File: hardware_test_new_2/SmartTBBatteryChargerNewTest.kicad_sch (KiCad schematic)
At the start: 130 parts, among them J3 XT60_MALE, J7 Conn_SWD, J8 Conn_01x02, Q3 AO3400A, Q4 BSC070N10NS5, U1 RY8411, U2 RS3236, U3 RY8411, U4 STM32G474RBTx, U5 INA180A1, U9 INA240A1PW, Y3 CSTCE8M

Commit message: New test channel schematic
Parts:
- removed C100, C101, C102, C103, C43, C44, C50, C51, C52, C58, C92, C93, C94, C95, C96, C97, C98, C99: 100n, Capacitor_SMD:C_0603_1608Metric, symbol Device:C
- removed C40, C42, C49: 100u, Capacitor_THT:CP_Radial_D6.3mm_P2.50mm, symbol Device:C_Polarized
- removed C45, C46, C59: 10u, Capacitor_SMD:C_1206_3216Metric, symbol Device:C
- removed D18, D19, D20, D21, D22, D23, D24, D25, D26, D27, D28, D29: WS2812B-2020, LED_SMD:LED_WS2812B-2020_PLCC4_2.0x2.0mm, symbol LED:WS2812B-2020
- removed D3: D_Schottky, Diode_SMD:D_PowerDI-5, symbol Device:D_Schottky
- removed F3: 5A, Fuse:Fuse_1206_3216Metric, symbol Device:Fuse
- removed J3: XT60_MALE, Connector_AMASS:AMASS_XT60-M_1x02_P7.20mm_Vertical, symbol Connector_Generic:Conn_01x02
- removed L4: 47u, Inductor_SMD:L_Coilcraft_MSS1260-XXX, symbol Device:L
- removed Q4: BSC070N10NS5, Package_TO_SOT_SMD:TDSON-8-1, symbol Transistor_FET:BSC070N10NS5
- removed R14: 10k, Resistor_SMD:R_0603_1608Metric, symbol Device:R
- removed R15: 90k, Resistor_SMD:R_0603_1608Metric, symbol Device:R
- removed R22: 33R, Resistor_SMD:R_0603_1608Metric, symbol Device:R
- removed R23: 4m, Resistor_SMD:R_Shunt_Vishay_WSK2512_6332Metric_T1.19mm, symbol Device:R_Shunt
- removed R28: 1R, Resistor_SMD:R_0603_1608Metric, symbol Device:R
- removed R5: 10m, Resistor_SMD:R_Shunt_Vishay_WSK2512_6332Metric_T1.19mm, symbol Device:R_Shunt
- removed U5: INA180A1, Package_TO_SOT_SMD:SOT-23-5, symbol Amplifier_Current:INA180A1
- removed U9: INA240A1PW, Package_SO:TSSOP-8_4.4x3mm_P0.65mm, symbol Amplifier_Current:INA240A1PW
- added C22: 10u, Capacitor_SMD:C_1206_3216Metric, symbol Device:C_Small
- added C24: 100n, Capacitor_SMD:C_0603_1608Metric, symbol Device:C_Small
- added D10: K34, Diode_SMD:D_SOD-123F, symbol Device:D_Schottky
- added U6: FD6288Q, Package_DFN_QFN:QFN-24-1EP_4x4mm_P0.5mm_EP2.7x2.7mm, symbol AEX7 Others:FD6288Q
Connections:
- net +10V: now also C22.1, D10.2 (A), U6.4 (VCC)
- net CHA_HG: now also U6.19 (HO1)
- net CHA_SW: now also C24.2, U6.18 (VS1)
- net GND: now also C22.2, U6.25 (EP), U6.6 (COM)
- net VPP: now also F8.1
- new net: C24.1, D10.1 (K), U6.20 (VB1)
- new net: U6.21 (NC), U6.5 (NC), U6.7 (NC), U6.8 (NC)
- new net CHA1_DRVH: U6.22 (HIN1)
- new net CHA2_DRVH: U6.23 (HIN2)
- new net CHB1_DRVH: U6.24 (HIN3)
- no-connect marks 36 -> 41
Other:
- added sheet ChannelA1 (channel1.kicad_sch)
- added sheet ChannelA2 (channel1.kicad_sch)
- moved on the sheet: JP1

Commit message: test2 schematic
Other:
- added sheet ChannelB1 (channel1.kicad_sch)
- added sheet ChannelB2 (channel1.kicad_sch)
- added sheet ChannelC1 (channel1.kicad_sch)
- added sheet ChannelC2 (channel1.kicad_sch)

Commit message: test2 schematic should ok
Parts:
- removed D4, D5, D6: LED, LED_SMD:LED_0603_1608Metric, symbol Device:LED
- removed Y3: CSTCE8M, Crystal:Resonator_SMD_Murata_CSTxExxV-3Pin_3.0x1.1mm_HandSoldering, symbol Device:Resonator
- added C101, C102, C103, C104, C105, C106, C107, C108, C109, C37, C38, C39: 100n, Capacitor_SMD:C_0603_1608Metric, symbol Device:C
- added C110, C111, C31, C32, C34, C35, C36: 100n, Capacitor_SMD:C_0603_1608Metric, symbol Device:C_Small
- added C33: 10u, Capacitor_SMD:C_1206_3216Metric, symbol Device:C_Small
- added D18, D19, D20, D21, D22: K34, Diode_SMD:D_SOD-123F, symbol Device:D_Schottky
- added D23, D24, D25, D26, D27, D28: LED_BLUE, LED_SMD:LED_0603_1608Metric, symbol Device:LED
- added D29, D30, D31, D4, D5, D6: WS2812B, LED_SMD:LED_WS2812B_PLCC4_5.0x5.0mm_P3.2mm, symbol LED:WS2812B
- added R12, R54, R56: 10k, Resistor_SMD:R_0603_1608Metric, symbol Device:R
- added R53, R55, R57, R64: 33, Resistor_SMD:R_0603_1608Metric, symbol Device:R
- added R58, R59, R60, R61, R62, R63: 2.2k, Resistor_SMD:R_0603_1608Metric, symbol Device:R
- added RN1, RN2: R_Pack04, Resistor_SMD:R_Array_Convex_4x0603, symbol Device:R_Pack04
- added SW1, SW2, SW3, SW4, SW5, SW6: SW_Push, Button_Switch_SMD:SW_SPST_SKQG_WithStem, symbol Switch:SW_Push
- added U12: FD6288Q, Package_DFN_QFN:QFN-24-1EP_4x4mm_P0.5mm_EP2.7x2.7mm, symbol AEX7 Others:FD6288Q
- J8: footprint Connector_AMASS:AMASS_XT30U-M_1x02_P5.0mm_Vertical -> Connector_AMASS:AMASS_XT60-M_1x02_P7.20mm_Vertical
- R13, R17: value 33r -> 33
- R16: value 33r -> 10k
- R3: value 53.6k -> 54.7k
- R30, R32: value 2.2k -> 10k
- R31: value 2.2k -> 33
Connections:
- net CHA_HG is gone; now on net CHA1_HG: U6.19 (HO1)
- net CHA_SW is gone; now on net CHA1_SW: C24.2, U6.18 (VS1)
- net DRV_CHA1 is gone; now on net +3.3V: R16.1
- net DRV_CHA2 is gone; now on net BTN1: R13.1
- net DRV_CHB is gone; now on net BTN2: R17.1
- net ISENSE_INPUT is gone; now on net VSENSE_INPUT: U4.8 (PC0)
- net +10V: now also C110.1, C111.1, C33.1, D18.2 (A), D19.2 (A), D20.2 (A), D21.2 (A), D22.2 (A), U12.4 (VCC)
- net +3.3V: now also R30.1, R32.1, R12.1, R54.1, R56.1
- net +5V: now also C104.2, C105.2, C106.2, C107.2, C108.2, C109.2, D29.1 (VDD), D30.1 (VDD), D31.1 (VDD), D4.1 (VDD), D5.1 (VDD), D6.1 (VDD)
- net CHA1_DRVH: now also U4.42 (PA8), R58.1, RN2.1 (R1.1); no longer U6.22 (HIN1)
- net CHA2_DRVH: now also U4.43 (PA9), R59.1, RN2.2 (R2.1); no longer U6.23 (HIN2)
- net CHA2_HG: now also U6.16 (HO2)
- net CHA2_SW: now also U6.15 (VS2), C31.2
- net CHB1_DRVH: now also U4.44 (PA10), R60.1, RN2.3 (R3.1); no longer U6.24 (HIN3)
- net CHB1_HG: now also U6.13 (HO3)
- net CHB1_SW: now also U6.12 (VS3), C32.2
- net CHB2_HG: now also U12.19 (HO1)
- net CHB2_SW: now also C34.2, U12.18 (VS1)
- net CHC1_HG: now also U12.16 (HO2)
- net CHC1_SW: now also C35.2, U12.15 (VS2)
- net CHC2_HG: now also U12.13 (HO3)
- net CHC2_SW: now also C36.2, U12.12 (VS3)
- net GND: now also C101.1, C102.1, C103.1, C104.1, C105.1, C106.1, C107.1, C108.1, C109.1, C110.2, C111.2, C33.2, C37.1, C38.1, C39.1, D23.1 (K), D24.1 (K), D25.1 (K), D26.1 (K), D27.1 (K), D28.1 (K), D29.3 (VSS), D30.3 (VSS), D31.3 (VSS), D4.3 (VSS), D5.3 (VSS), D6.3 (VSS), SW1.2, SW2.2, SW3.2, SW4.2, SW5.2, SW6.2, U12.25 (EP), U12.6 (COM)
- net RGB_DATA: now also U4.57 (PB4), R64.1; no longer U4.45 (PA11)
- net VSENSE_INPUT: no longer U4.35 (PB13)
- net CHB2_VS: now reaches U4.11 (PC3)
- net CHB1_VS: now reaches U4.12 (PA0)
- net CHA2_VS: now reaches U4.13 (PA1)
- net CHA1_VS: now reaches U4.14 (PA2)
- net CHC2_IS: now reaches U4.19 (PA5)
- net CHC1_IS: now reaches U4.20 (PA6)
- net CHB1_IS: now reaches U4.22 (PC4)
- net CHA2_IS: now reaches U4.23 (PC5)
- net CHA1_IS: now reaches U4.26 (PB2)
- net CHC2_DRVH: now reaches U4.34 (PB12)
- net CHC2_DRVH: now also R63.1, RN1.3 (R3.1)
- net BTN6: now reaches U4.55 (PD2)
- net BTN6: now also C103.2, R57.1
- net BTN5: now reaches U4.56 (PB3)
- net BTN5: now also C102.2, R55.1
- net BTN4: now reaches U4.58 (PB5)
- net BTN4: now also C101.2, R53.1
- net BTN3: now reaches U4.59 (PB6)
- net BTN3: now also R31.1, C39.2
- net BTN2: now reaches U4.60 (PB7)
- net BTN2: now also C38.2
- net BTN1: now reaches U4.62 (PB9)
- net BTN1: now also C37.2
- net at U6.14 (VB3): now also C32.1, D19.1 (K)
- net at U6.17 (VB2): now also C31.1, D18.1 (K)
- net at R31.2: now also R30.2, SW3.1
- net at R32.2: now also R53.2, SW4.1
- net ISENSE_CHA renamed CHC1_VS
- net ISENSE_CHB renamed CHC2_VS
- net VSENSE_CHA renamed CHB2_IS
- net VSENSE_CHB: no longer names the net of U4.24 (PB0)
- new net: R56.2, R57.2, SW6.1
- new net: R16.2, R17.2, SW2.1
- new net: C36.1, D22.1 (K), U12.14 (VB3)
- new net: C34.1, D20.1 (K), U12.20 (VB1)
- new net: D25.2 (A), R60.2
- new net: D27.2 (A), R62.2
- new net: C35.1, D21.1 (K), U12.17 (VB2)
- new net: D29.2 (DOUT), D30.4 (DIN)
- new net: D29.4 (DIN), D6.2 (DOUT)
- new net: D4.2 (DOUT), D5.4 (DIN)
- new net: D4.4 (DIN), R64.2
- new net: D28.2 (A), R63.2
- new net: RN2.8 (R1.2), U6.22 (HIN1)
- new net: RN2.7 (R2.2), U6.23 (HIN2)
- new net: RN2.6 (R3.2), U6.24 (HIN3)
- new net: RN1.6 (R3.2), U12.24 (HIN3)
- new net: RN1.7 (R2.2), U12.23 (HIN2)
- new net: RN1.8 (R1.2), U12.22 (HIN1)
- new net: D26.2 (A), R61.2
- new net: D24.2 (A), R59.2
- new net: D5.2 (DOUT), D6.4 (DIN)
- new net: R12.2, R13.2, SW1.1
- new net: U12.21 (NC), U12.5 (NC), U12.7 (NC), U12.8 (NC)
- new net: D23.2 (A), R58.2
- new net: R54.2, R55.2, SW5.1
- new net: D30.2 (DOUT), D31.4 (DIN)
- new net CHB2_DRVH: R61.1, RN1.1 (R1.1), U4.45 (PA11)
- new net CHC1_DRVH: R62.1, RN1.2 (R2.1), U4.35 (PB13)
- no-connect marks 41 -> 44
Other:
- sheet ChannelA1 ports: added CH_VOUT; removed none
- sheet ChannelA2 ports: added CH_VOUT; removed none
- sheet ChannelB1 ports: added CH_VOUT; removed none
- sheet ChannelB2 ports: added CH_VOUT; removed none
- sheet ChannelC1 ports: added CH_VOUT; removed none
- sheet ChannelC2 ports: added CH_VOUT; removed none
- moved on the sheet: BZ1, C22, C24, C53, C54, C55, C56, D10, D9, F8, FB1, J8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

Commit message: layout half done
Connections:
- net +3.3V: no longer C90.2, C91.2, U4.28 (VREF+)
- new net VREF: C90.2, C91.2, U4.28 (VREF+)
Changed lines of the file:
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@@
 	(wire
 		(pts
-			(xy 60.96 45.72) (xy 57.15 45.72)
-		)
-		(stroke
-			(width 0)
-			(type default)
-		)
-	)
-	(wire
-		(pts
 			(xy 186.69 254) (xy 193.04 254)
 		)
@@
 	(wire
 		(pts
+			(xy 57.15 45.72) (xy 58.42 45.72)
+		)
+		(stroke
+			(width 0)
+			(type default)
+		)
+	)
+	(wire
+		(pts
 			(xy 36.83 30.48) (xy 34.29 30.48)
 		)
@@
 		)
 	)
+	(label "VREF"
+		(at 58.42 45.72 0)
+		(effects
+			(font
+				(size 1.27 1.27)
+			)
+			(justify left bottom)
+		)
+	)
 	(global_label "CHC2_SW"
 		(shape input)
@@
 					(unit 1)
 				)
-			)
-		)
-	)
-	(symbol
-		(lib_id "power:+3.3V")
-		(at 60.96 45.72 0)
-		(unit 1)
-		(exclude_from_sim no)
-		(in_bom yes)
-		(on_board yes)
-		(dnp no)
-		(fields_autoplaced yes)
-		(property "Reference" "#PWR018"
-			(at 60.96 49.53 0)
-			(effects
-				(font
-					(size 1.27 1.27)
-				)
-				(hide yes)
-			)
-		)
-		(property "Value" "+3.3V"
-			(at 60.96 40.64 0)
-			(effects
-				(font
-					(size 1.27 1.27)
-				)
-			)
-		)
-		(property "Footprint" ""
-			(at 60.96 45.72 0)
-			(effects
-				(font
-					(size 1.27 1.27)
-				)
-				(hide yes)
-			)
-		)
-		(property "Datasheet" ""
-			(at 60.96 45.72 0)
-			(effects
-				(font
-					(size 1.27 1.27)
-				)
-				(hide yes)
-			)
-		)
-		(property "Description" "Power symbol creates a global label with name \"+3.3V\""
-			(at 60.96 45.72 0)
-			(effects
-				(font
-					(size 1.27 1.27)
-				)
-				(hide yes)
-			)
-		)
-		(pin "1"
-		)
-		(instances
-			(project "SmartTBBatteryChargerNewTest"
-				(path "/2e05ddd5-7934-49df-b3d1-7d213e2935b6"
-					(reference "#PWR018")
-					(unit 1)
-				)

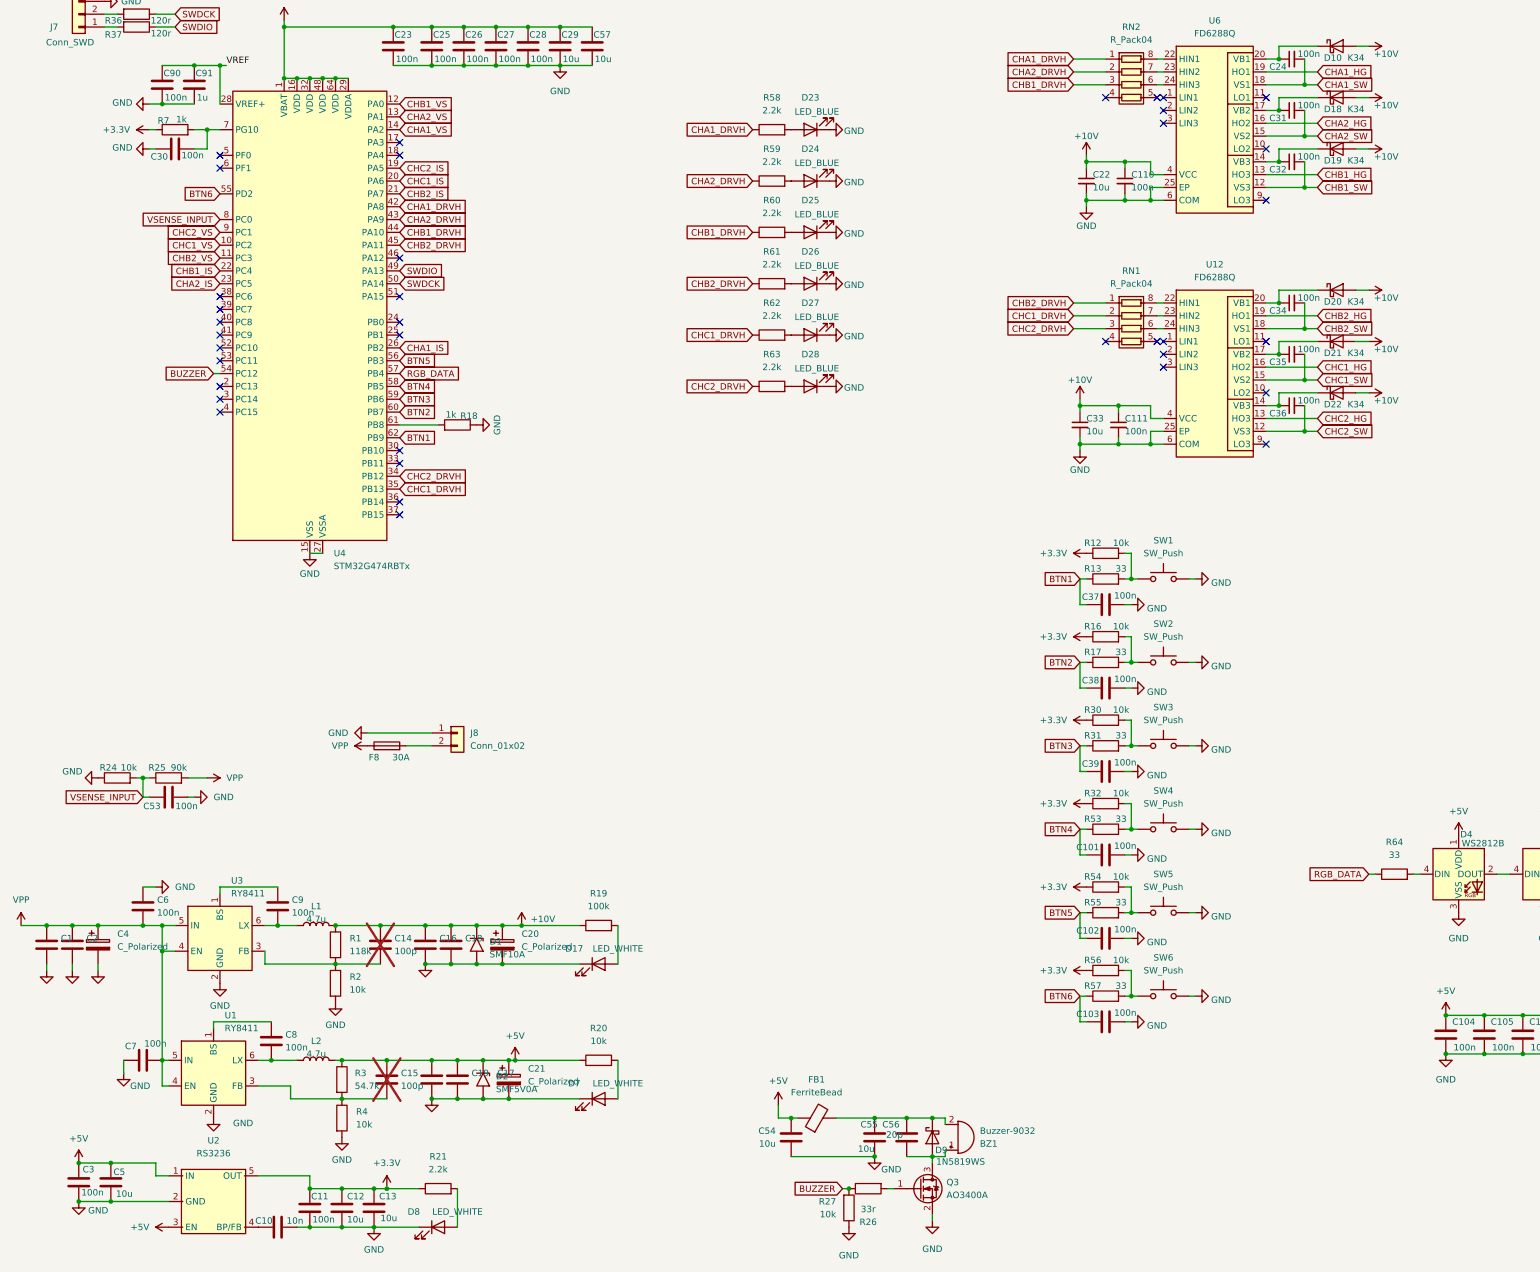
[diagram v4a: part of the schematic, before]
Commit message: new Hardware manufactured
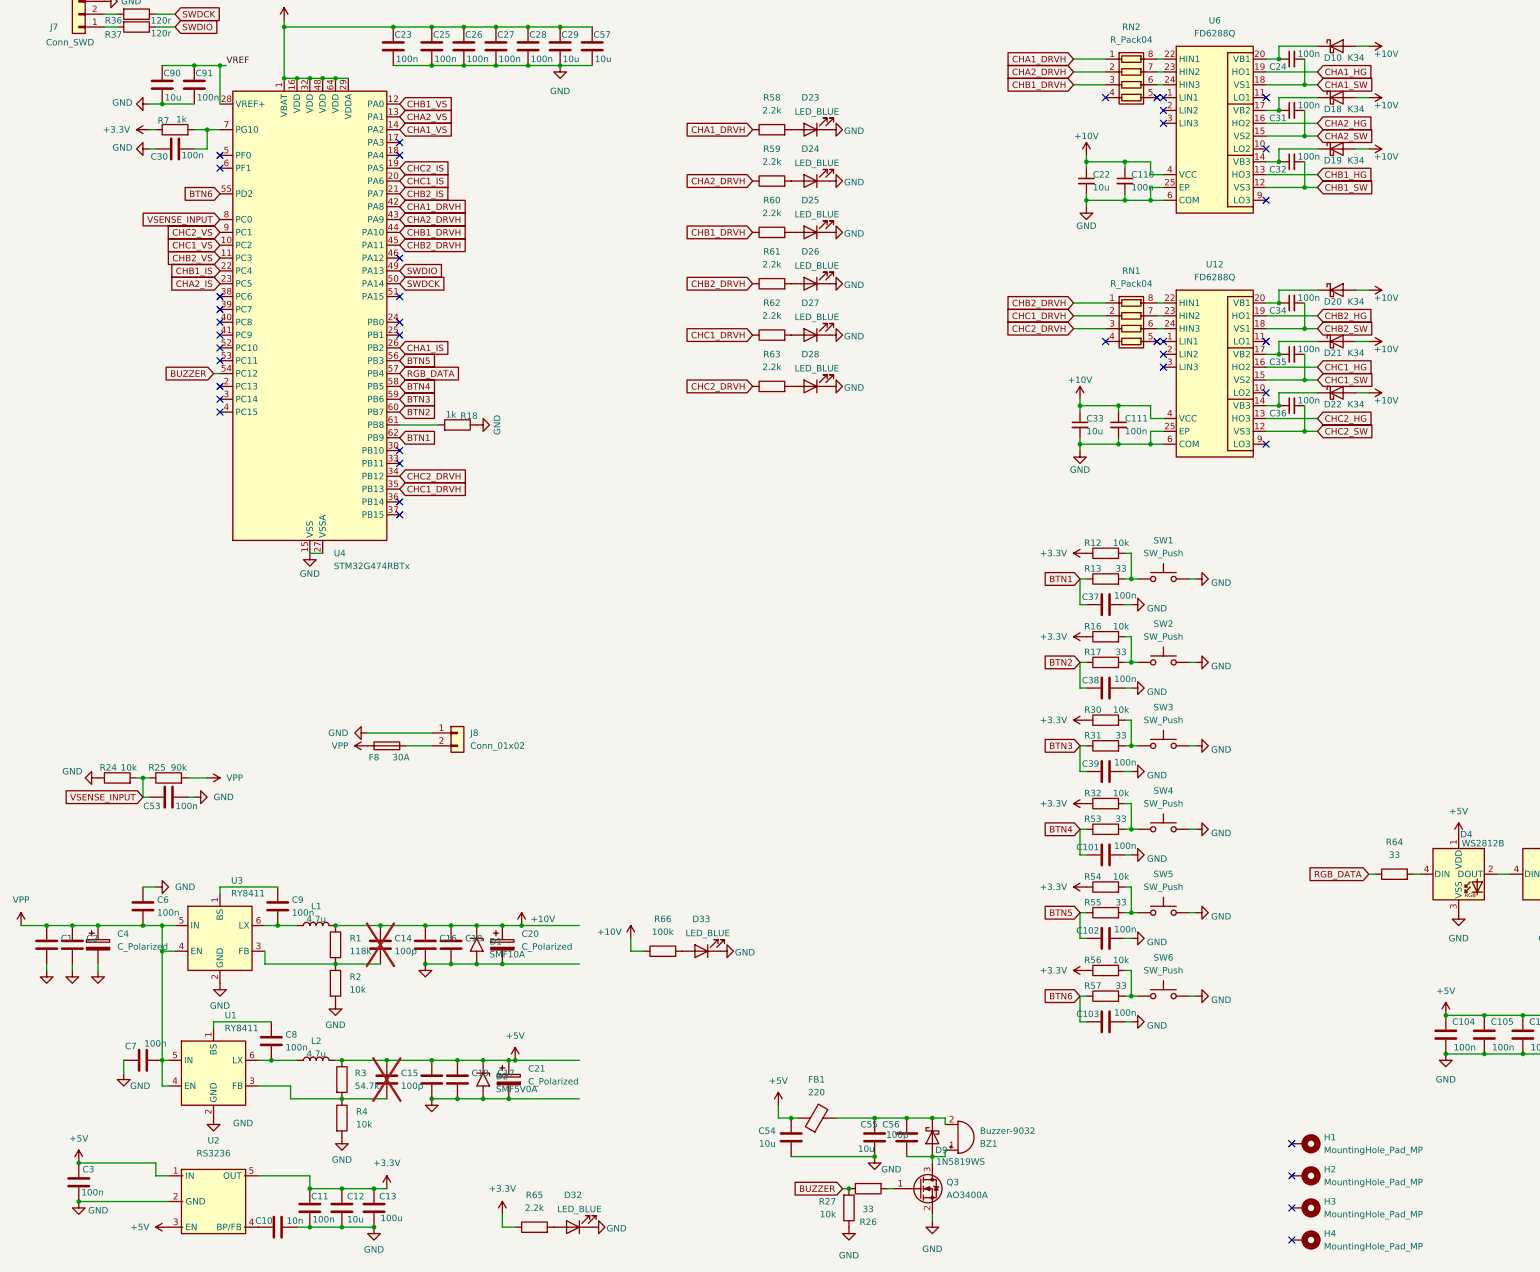
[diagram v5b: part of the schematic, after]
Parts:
- removed C5: 10u, Capacitor_SMD:C_0603_1608Metric, symbol Device:C
- removed D17, D7, D8: LED_WHITE, LED_SMD:LED_0603_1608Metric, symbol Device:LED
- removed R19: 100k, Resistor_SMD:R_0603_1608Metric, symbol Device:R
- removed R20: 10k, Resistor_SMD:R_0603_1608Metric, symbol Device:R
- removed R21: 2.2k, Resistor_SMD:R_0603_1608Metric, symbol Device:R
- added D32, D33: LED_BLUE, LED_SMD:LED_0603_1608Metric, symbol Device:LED
- added H1, H2, H3, H4: MountingHole_Pad_MP, MountingHole:MountingHole_3.2mm_M3_DIN965_Pad_TopBottom, symbol Mechanical:MountingHole_Pad_MP
- added R65: 2.2k, Resistor_SMD:R_0603_1608Metric, symbol Device:R
- added R66: 100k, Resistor_SMD:R_0603_1608Metric, symbol Device:R
- C13: value 10u -> 100u; footprint Capacitor_SMD:C_0603_1608Metric -> Capacitor_SMD:C_1206_3216Metric
- C20, C21: footprint Capacitor_THT:CP_Radial_D6.3mm_P2.50mm -> Capacitor_THT:CP_Radial_D5.0mm_P2.00mm
- C56: value 20p -> 100p
- C90: value 100n -> 10u
- C91: value 1u -> 100n
- FB1: value FerriteBead -> 220
- R26: value 33r -> 33
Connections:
- net +10V: now also R66.1
- net +3.3V: now also R65.1
- net GND: now also D32.1 (K), D33.1 (K)
- new net: D32.2 (A), R65.2
- new net: D33.2 (A), R66.2
- no-connect marks 44 -> 48
